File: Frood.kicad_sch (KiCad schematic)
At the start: 43 parts, among them J1 Conn_02x13+5, SW1 RESET, SW2 BOOT, U1 RP2040, U2 W25Q32JVUUIQ, U3 SPX3819M5-L-3-3/TR, Y1 TXM12M0004252LBCEO00T

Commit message: Rev8 update
* Add a 2-way solder jumper to select VBUS OUT or VBUS IN on the RAW pin
* Use orange indicator LED again
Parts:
- added JP3: VBUS_SEL, 42keebs:SolderJumper-3_P1.3mm_Bridged12_RoundedPad0.8x1mm, symbol Jumper:Jumper_3_Bridged12
- D2: LCSC C130719 -> (none)
- J1, JP1, JP2: now left out of the parts list
- R9: LCSC C11702 -> (none)
- SW1, SW2: LCSC C2845235 -> (none)
- U2: LCSC C2999380 -> (none)
- Y1: PartNo C284156 -> (none)
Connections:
- net RAW: now also JP3.2 (C); no longer C1.1, D1.1 (K), U3.1 (IN), U3.3 (EN)
- net VBUS: now also JP3.3 (B)
- net VSENSE: now reaches R11.1, R12.2, U1.30 (GPIO19)
- new net VBUS_OUT: C1.1, D1.1 (K), JP3.1 (A), U3.1 (IN), U3.3 (EN)

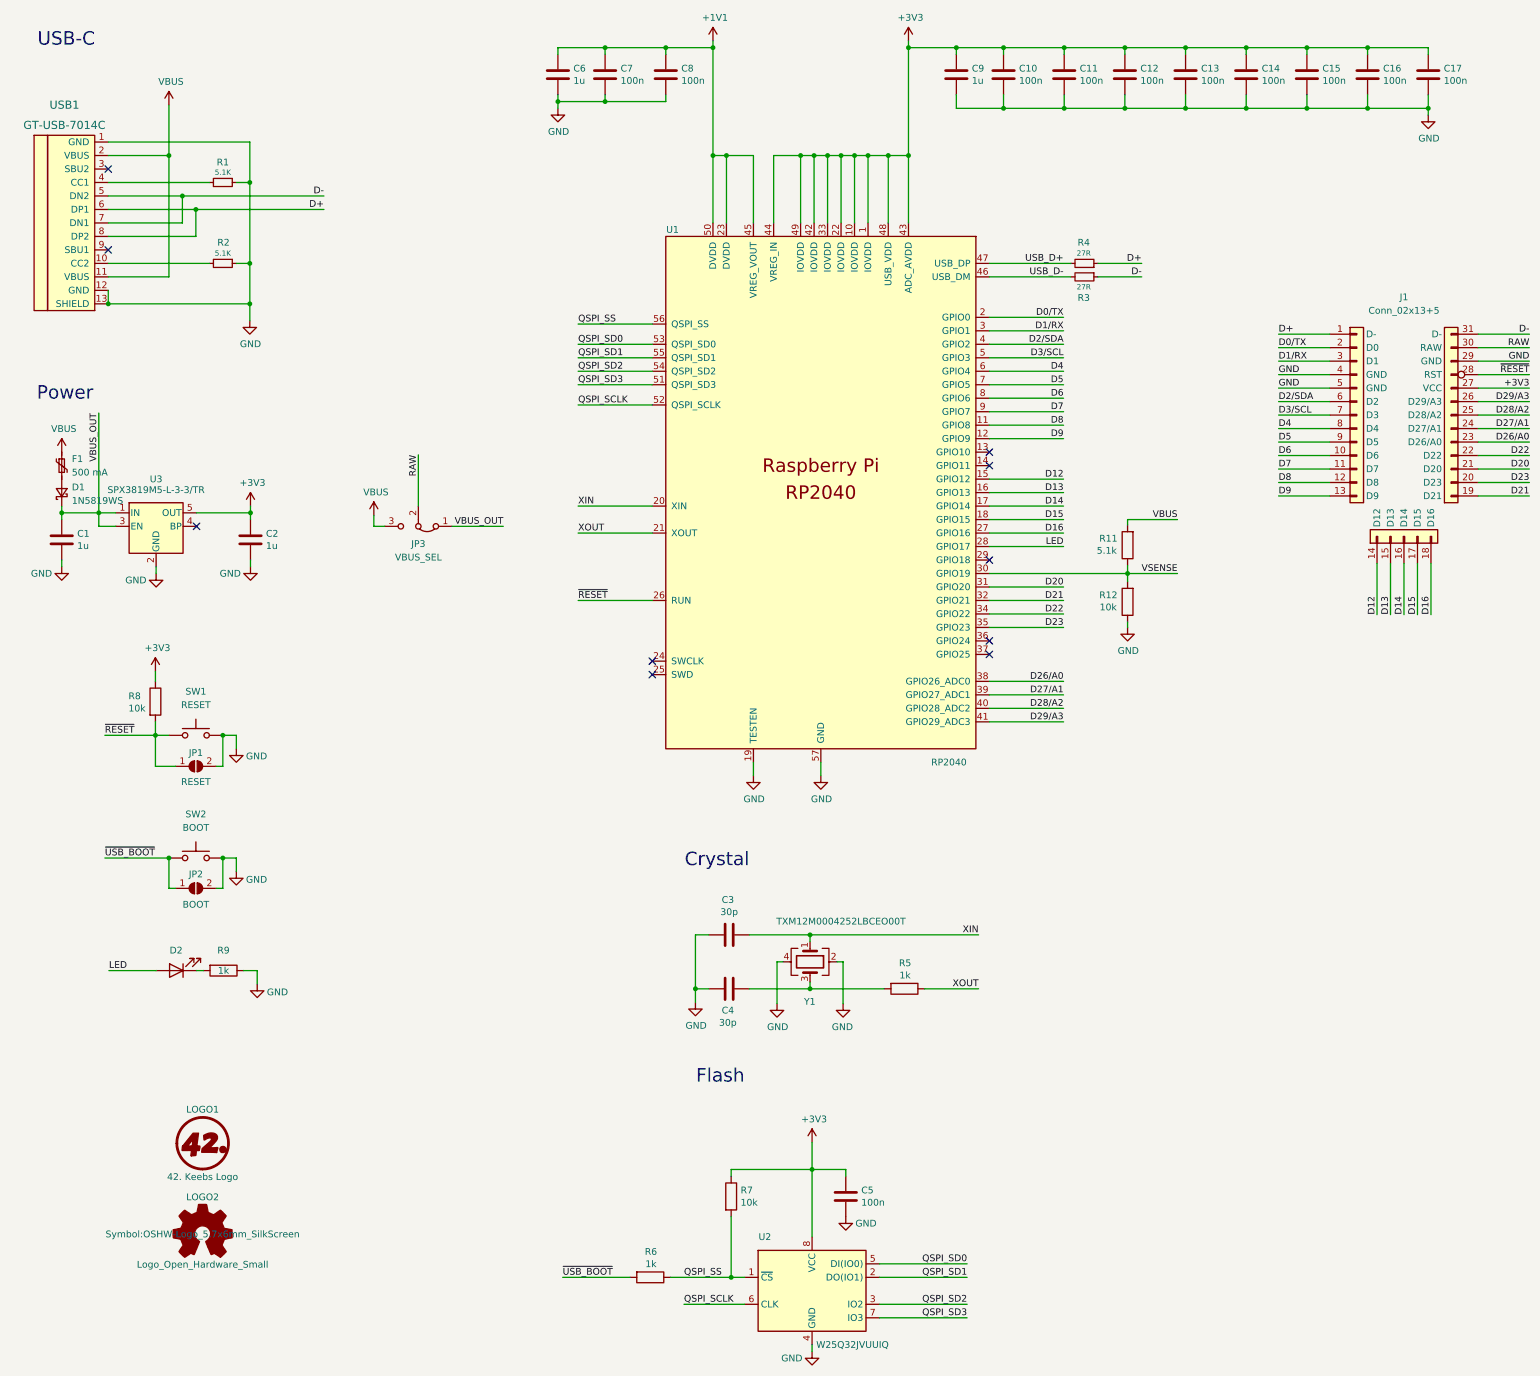
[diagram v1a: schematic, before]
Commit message: Rev9 update
* Allows converting left-hand side GND pins into GPIO10,11 pins
* Drop VBUS IN/OUT solder jumper, RAW pin now connected between the Schottky and fuse/regulator
* Uses a different (but equivalent) USB-C socket
* Routing and silkscreen tweaks/improvements
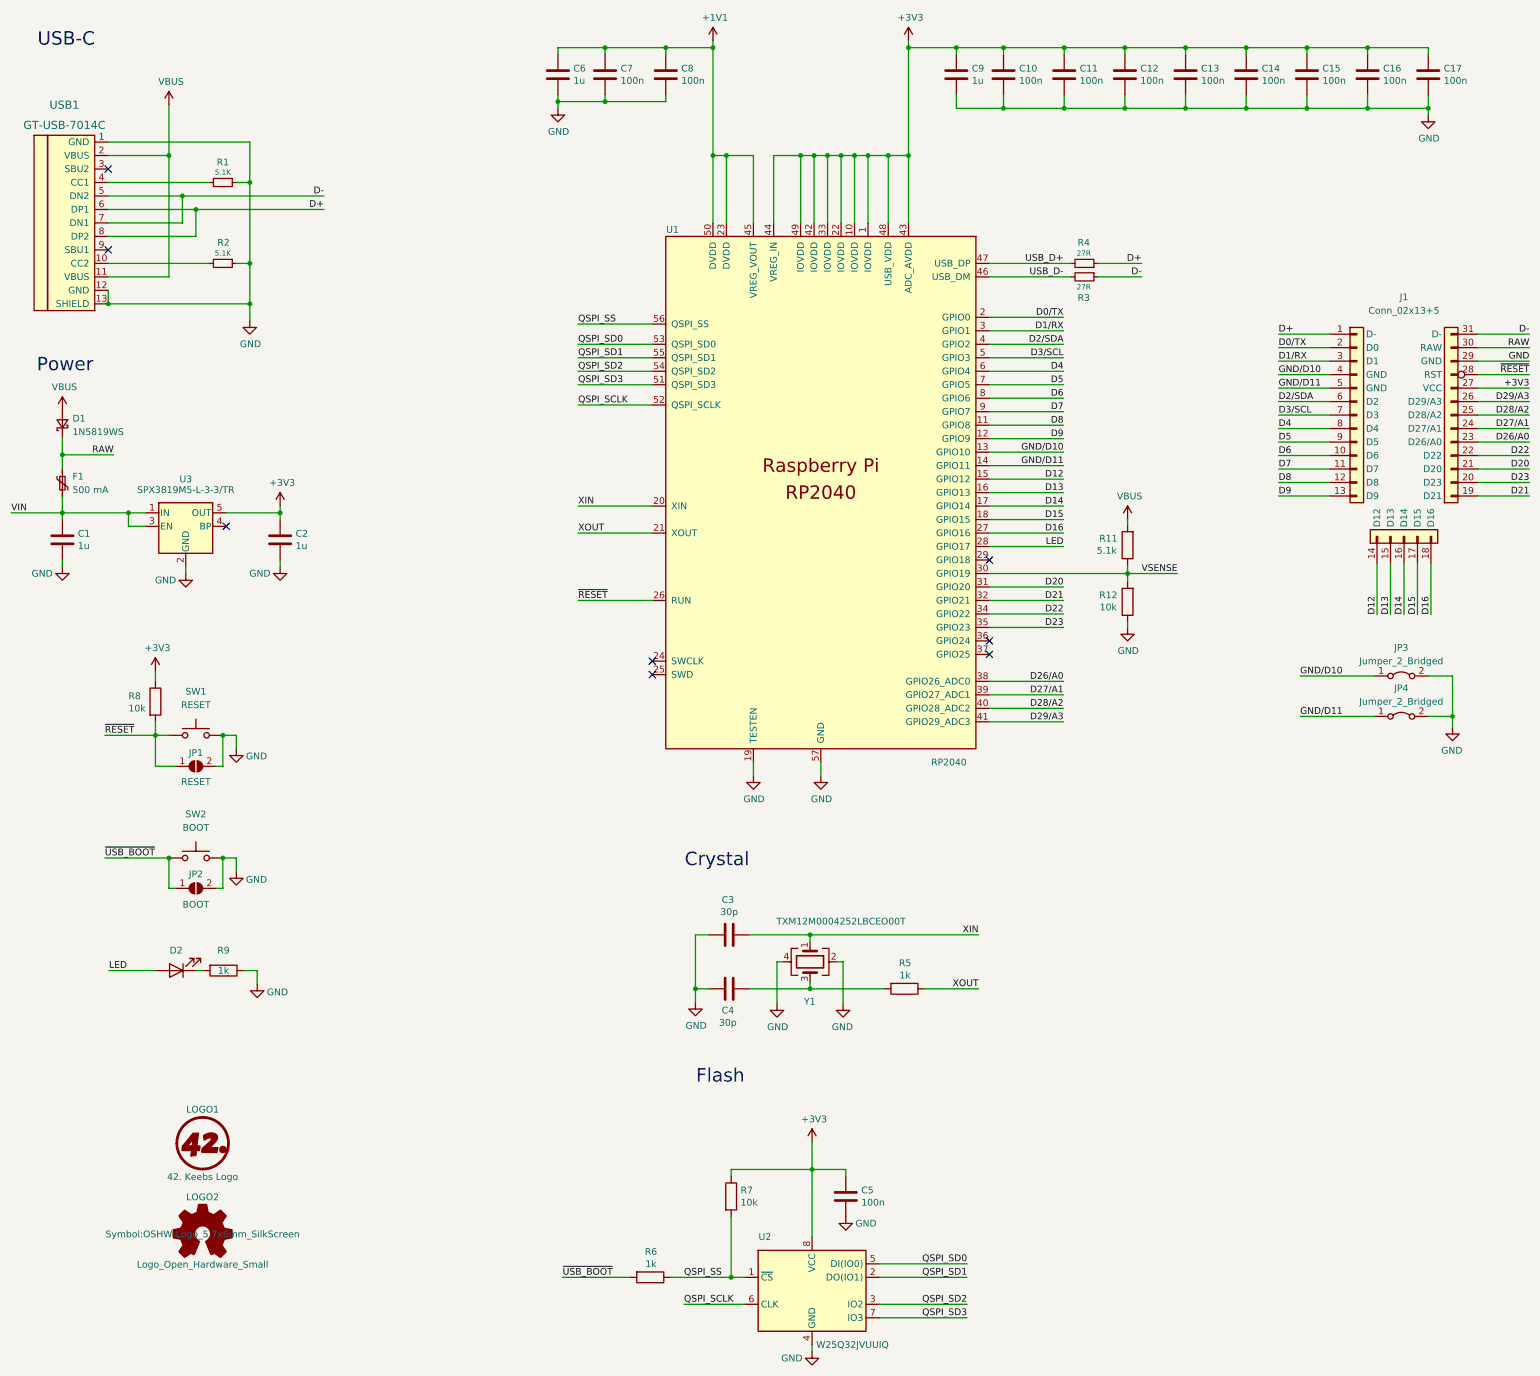
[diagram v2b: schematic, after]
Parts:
- removed JP3: VBUS_SEL, 42keebs:SolderJumper-3_P1.3mm_Bridged12_RoundedPad0.8x1mm, symbol Jumper:Jumper_3_Bridged12
- added JP3, JP4: Jumper_2_Bridged, 42keebs:SolderJumper-2_P0.8mm_Bridged_RoundedPad0.5x1mm, symbol Jumper:Jumper_2_Bridged
- J1: footprint 42keebs:PinHeader_2x13+5_P2.54mm_Vertical_Elite-C -> 42keebs:PinHeader_2x13+5_P2.54mm_Vertical_Frood
- SW1, SW2: footprint Button_Switch_SMD:SW_SPST_CK_KXT3 -> 42keebs:SW_SPST_CK_KXT3
- USB1: footprint 42keebs:Molex-216990_GCT-USB45xx_HRO-TYPE-C-31-M-13x-PiMicro -> 42keebs:Molex-216990_GCT-USB45xx_HRO-TYPE-C-31-M-13x-Frood
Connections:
- net GND: now also JP3.2 (B), JP4.2 (B); no longer J1.4 (GND), J1.5 (GND)
- net RAW: now also D1.1 (K), F1.1
- net VBUS: now also D1.2 (A); no longer F1.1
- net VIN: now reaches F1.2
- net VIN: now also C1.1, U3.1 (IN), U3.3 (EN); no longer D1.2 (A)
- net GND/D10: now reaches U1.13 (GPIO10)
- net GND/D10: now also J1.4 (GND), JP3.1 (A)
- net GND/D11: now reaches U1.14 (GPIO11)
- net GND/D11: now also J1.5 (GND), JP4.1 (A)
- removed net VBUS_OUT: C1.1, D1.1 (K), U3.1 (IN), U3.3 (EN)
- no-connect marks 10 -> 8
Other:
- moved on the sheet: C2, D1, F1, U3
